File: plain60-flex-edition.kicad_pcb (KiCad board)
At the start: 2 copper layers, 284.7 x 94.2 mm, 171 parts, among them J1 4P4C, K1 KEYSW, K10 KEYSW, K11 KEYSW, K12 KEYSW, K13 KEYSW, K14 KEYSW, K15 KEYSW, K15-1 KEYSW, K16 KEYSW, K17 KEYSW, K18 KEYSW, K19 KEYSW, K2 KEYSW, K20 KEYSW, K21 KEYSW, K22 KEYSW, K23 KEYSW, K24 KEYSW, K25 KEYSW, K26 KEYSW, K27 KEYSW, K28 KEYSW, K29 KEYSW, K3 KEYSW, K31 KEYSW, K31-1 KEYSW, K32 KEYSW, K33 KEYSW, K34 KEYSW, K35 KEYSW, K36 KEYSW, K37 KEYSW, K38 KEYSW, K39 KEYSW, K4 KEYSW, K40 KEYSW, K41 KEYSW, K42 KEYSW, K43 KEYSW, K44 KEYSW, K44-1 KEYSW, K46 KEYSW, K47 KEYSW, K48 KEYSW, K49 KEYSW, K5 KEYSW, K50 KEYSW, K51 KEYSW, K52 KEYSW, K53 KEYSW, K54 KEYSW, K55 KEYSW, K56 KEYSW, K57 KEYSW, K58 KEYSW, K58-1 KEYSW, K59 KEYSW, K6 KEYSW, K61 KEYSW, K61-1 KEYSW, K62 KEYSW, K62-1 KEYSW, K63 KEYSW, K63-1 KEYSW, K67 KEYSW, K67-1 KEYSW, K7 KEYSW, K71 KEYSW, K72 KEYSW, K72-1 KEYSW, K73 KEYSW, K73-1 KEYSW, K74 KEYSW, K74-1 KEYSW, K8 KEYSW, K9 KEYSW, U1 ProS3

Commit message: fix pins
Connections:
- U1 pad 11: unconnected-(U1-Pad11) -> col9
- U1 pad 12: col9 -> unconnected-(U1-Pad12)
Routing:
- net col9: track 359.2 -> 360.3 mm
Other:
- board text added: "NEED FIX"

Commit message: fix pins
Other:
- board text removed: "NEED FIX"
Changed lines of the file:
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@@
   (gr_line (start 2.525008 0.525008) (end 7.525008 0.525008) (layer "Edge.Cuts") (width 0.1))
   (gr_line (start 13.825008 0.525008) (end 96.325008 0.525008) (layer "Edge.Cuts") (width 0.1))
-  (gr_text "NEED FIX" (at 22.869287 32.798061) (layer "B.Cu")
-    (effects (font (size 1.5 1.5) (thickness 0.3)) (justify mirror))
-  )
   (gr_text "based on Plain60 rev2.2" (at 98.821958 39.290658) (layer "B.SilkS")
     (effects (font (size 1 1) (thickness 0.15)) (justify mirror))

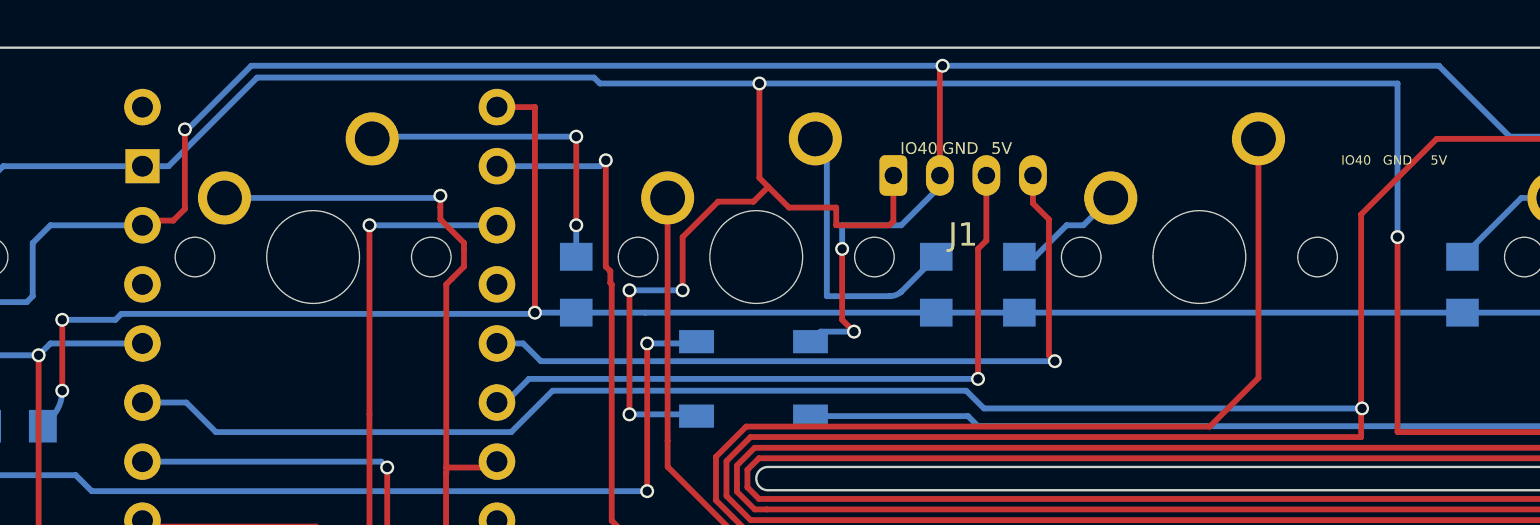
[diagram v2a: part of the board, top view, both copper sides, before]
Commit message: fixed JST header direction
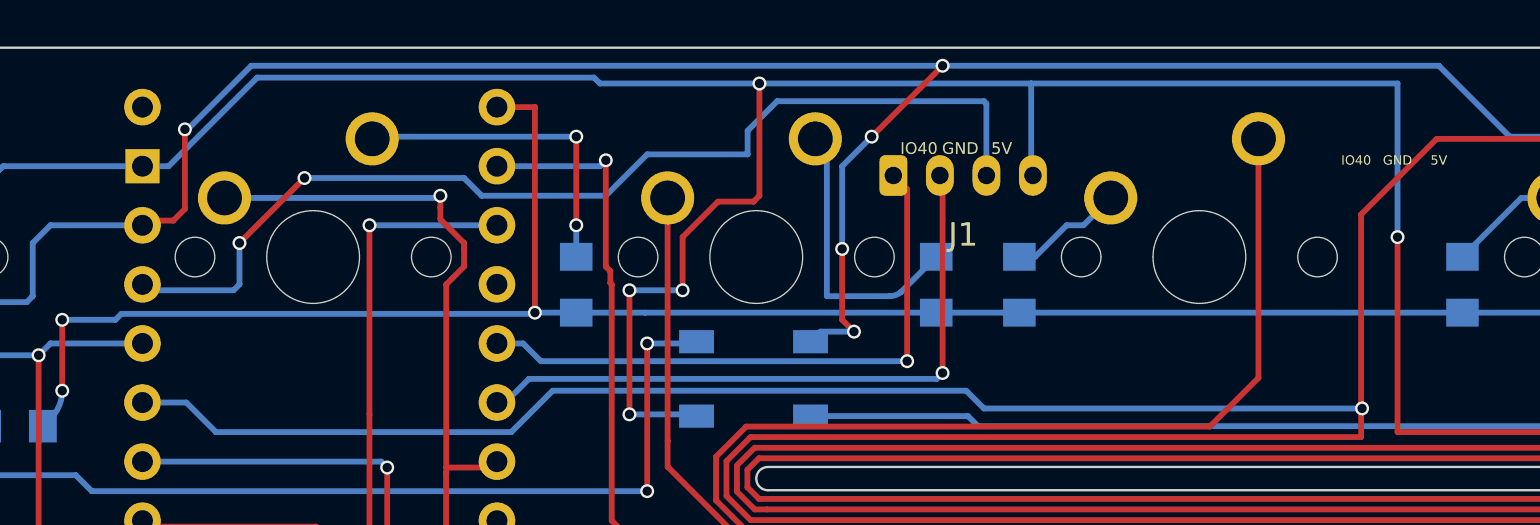
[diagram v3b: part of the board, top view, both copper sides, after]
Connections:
- D32 pad 2: Net-(D31-Pad2) -> Net-(D32-Pad2)
- J1 pad 1: GND -> display SCL
- J1 pad 2: 5V -> display SDA
- J1 pad 3: display SDA -> 3v3
- J1 pad 4: display SCL -> GND
- K31 pad 1: Net-(D32-Pad2) -> Net-(D31-Pad2)
- K31 pad 2: col1 -> col0
- K32 pad 1: Net-(D31-Pad2) -> Net-(D32-Pad2)
- K32 pad 2: col0 -> col1
- U1 pad 4: unconnected-(U1-Pad4) -> 3v3
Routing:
- net 3v3: track 0.00 -> 45.2 mm, vias 0 -> 2
- net Net-(D32-Pad2): track 0.00 -> 43.8 mm
- net Net-(D31-Pad2): track 57.1 -> 13.3 mm
- net display SCL: track 32.7 -> 26.2 mm
- net GND: track 708.9 -> 704.1 mm
- net 5V: track 694.9 -> 693.4 mm, vias 14 -> 15
- net display SDA: track 30.0 -> 28.9 mm
